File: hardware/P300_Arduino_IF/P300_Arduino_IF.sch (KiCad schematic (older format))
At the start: 30 parts, among them J1 Relay brd, J10 Pressure, J11 TGS2600, J12 I2C, J13 CO2, J14 5V, J15 TFT Display 1, J16 TFT Display 2, J2 DHT1, J3 DHT2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

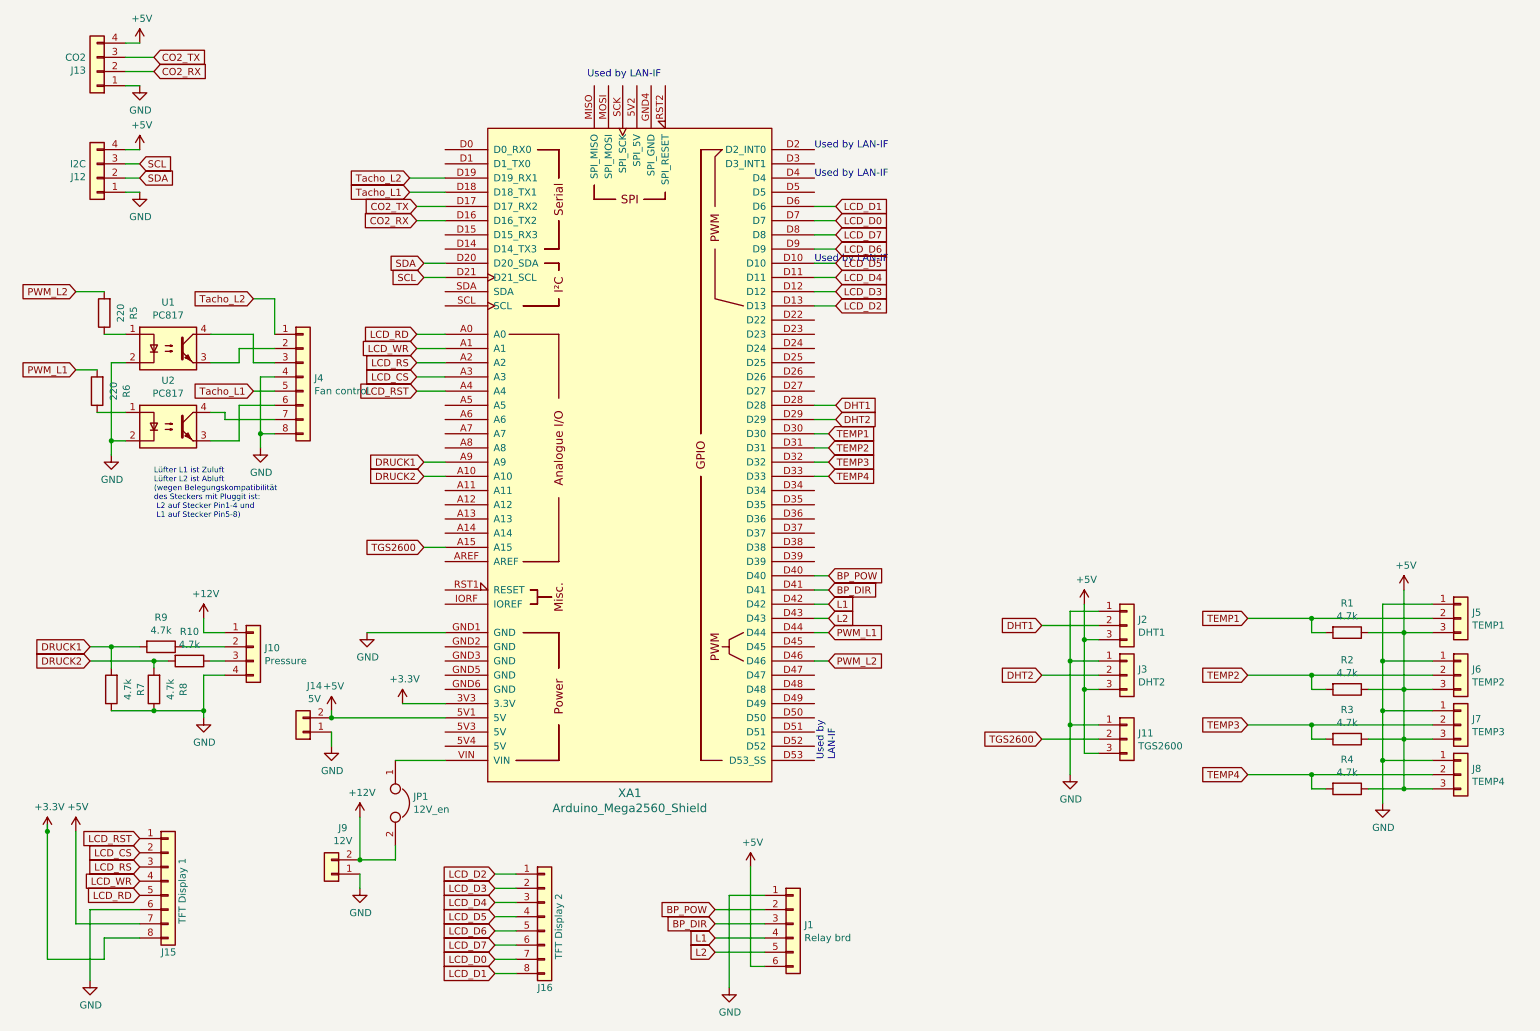
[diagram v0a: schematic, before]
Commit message: Platinen Update
Änderungen von HW-0.25 zu HW-0.26 - P300_Arduino_IF
 - Korrektur externer Displayanschluss zum Arduino

Änderungen von HW-0.23 zu HW-0.26 - P300_Display_IF
 - Korrektur Displayanschluss zum Display
 
Änderungen von HW-0.23 zu HW-0.25 - P300_Arduino_IF
 - Ergänzung von externen Pullup-Widerstand und Glättungskondensator am Tachosignal
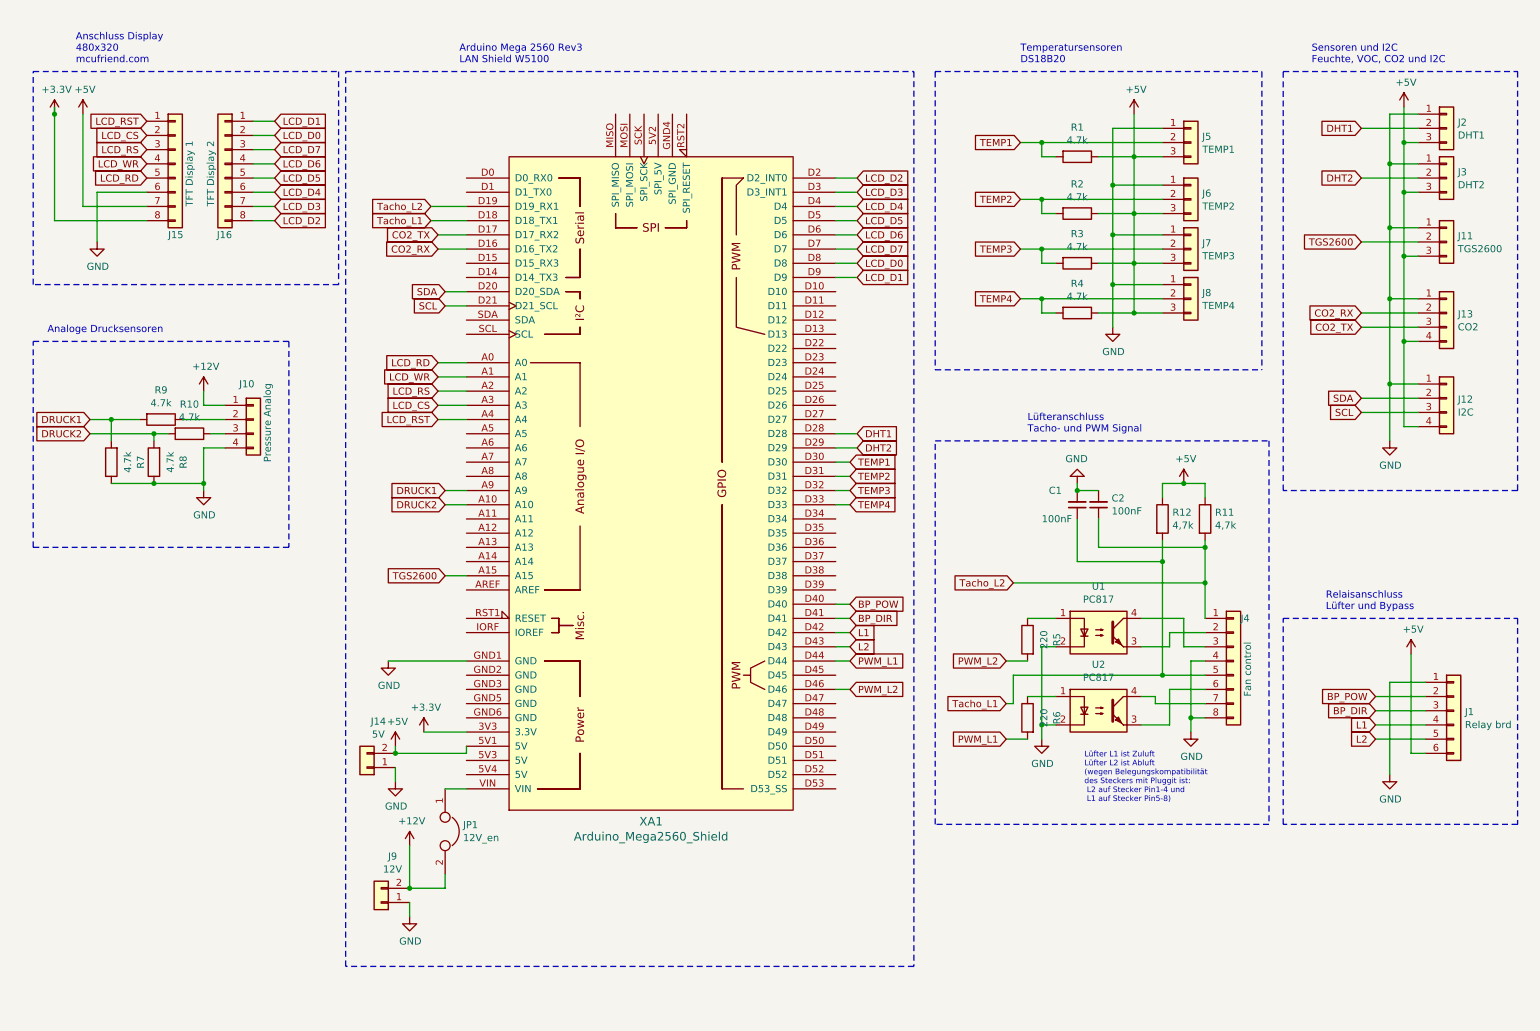
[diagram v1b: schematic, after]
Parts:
- added C1, C2: 100nF, Capacitors_THT:C_Disc_D5.0mm_W2.5mm_P5.00mm, symbol Device:C_Small
- added R11, R12: 4,7k, Resistors_THT:R_Axial_DIN0207_L6.3mm_D2.5mm_P2.54mm_Vertical, symbol Device:R
- J10: value Pressure -> Pressure Analog
- J15: footprint Connector_Molex:Molex_KK-6410-08_08x2.54mm_Straight -> Connectors_Molex:Molex_KK-6410-08_08x2.54mm_Straight
- J16: footprint Connector_Molex:Molex_KK-254_AE-6410-08A_1x08_P2.54mm_Vertical -> Connectors_Molex:Molex_KK-6410-08_08x2.54mm_Straight
- R1, R2, R3, R4: footprint Resistors_THT:R_Axial_DIN0207_L6.3mm_D2.5mm_P10.16mm_Horizontal -> Resistors_THT:R_Axial_DIN0207_L6.3mm_D2.5mm_P2.54mm_Vertical
- XA1: footprint Arduino:Arduino_Mega2560_Shield_no_ICSP -> Arduino_Mega2560_Shield
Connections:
- net +5V: now also R11.1, R12.1
- net GND: now also C1.2, C2.2
- net LCD_D0: now also J16.2 (Pin_2), XA1.D8; no longer J16.7 (Pin_7), XA1.D7
- net LCD_D1: now also J16.1 (Pin_1), XA1.D9; no longer J16.8 (Pin_8), XA1.D6
- net LCD_D2: now also J16.8 (Pin_8), XA1.D2 (D2_INT0); no longer J16.1 (Pin_1), XA1.D13
- net LCD_D3: now also J16.7 (Pin_7), XA1.D3 (D3_INT1); no longer J16.2 (Pin_2), XA1.D12
- net LCD_D4: now also J16.6 (Pin_6), XA1.D4; no longer J16.3 (Pin_3), XA1.D11
- net LCD_D5: now also J16.5 (Pin_5), XA1.D5; no longer J16.4 (Pin_4), XA1.D10
- net LCD_D6: now also J16.4 (Pin_4), XA1.D6; no longer J16.5 (Pin_5), XA1.D9
- net LCD_D7: now also J16.3 (Pin_3), XA1.D7; no longer J16.6 (Pin_6), XA1.D8
- net Tacho_L1: now also C1.1, R12.2
- net Tacho_L2: now also C2.1, R11.2
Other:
- note added: "Analoge Drucksensoren"
- note added: "Anschluss Display\n480x320\nmcufriend.com"
- note added: "Arduino Mega 2560 Rev3\nLAN Shield W5100"
- note added: "Lüfteranschluss\nTacho- und PWM Signal"
- note added: "Relaisanschluss\nLüfter und Bypass"
- note added: "Sensoren und I2C\nFeuchte, VOC, CO2 und I2C"
- note added: "Temperatursensoren\nDS18B20"
- note removed: "Used by LAN-IF"
- note removed: "Used by \nLAN-IF"
- moved on the sheet: J1, J10, J11, J12, J13, J14, J15, J16, J2, J3, J4, J5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
